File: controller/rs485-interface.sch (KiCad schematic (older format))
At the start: 4 parts

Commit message: Add more stuff to controller, start sourcing parts
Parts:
- gave numbers to parts that had none: 4
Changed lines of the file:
@@
 LIBS:mic-parts
 LIBS:controller-cache
-LIBS:line-interface-cache
 EELAYER 26 0
 EELAYER END
 $Descr A4 11693 8268
 encoding utf-8
-Sheet 4 6
+Sheet 3 10
 Title "Digital soil moisture sensor"
 Date "Tue 17 Feb 2015"
@@
 $EndDescr
 $Comp
-L SP3481EN U?
+L SP3481EN U3
 U 1 1 58C048AA
 P 6000 3600
-F 0 "U?" H 5700 3950 50  0000 L CNN
+F 0 "U3" H 5700 3950 50  0000 L CNN
 F 1 "SN65HVD72" H 6100 3950 50  0000 L CNN
 F 2 "Housings_SOIC:SOIC-8_3.9x4.9mm_Pitch1.27mm" H 6000 3600 50  0001 C CIN
@@
 $EndComp
 $Comp
-L C C?
+L C C20
 U 1 1 58C048AB
 P 4800 2700
-F 0 "C?" H 4850 2800 50  0000 L CNN
+F 0 "C20" H 4850 2800 50  0000 L CNN
 F 1 "1u" H 4850 2600 50  0000 L CNN
 F 2 "Capacitors_SMD:C_0603" H 4838 2550 30  0001 C CNN
@@
 Connection ~ 6000 4150
 $Comp
-L CONN_01X04 J?
+L CONN_01X04 J21
 U 1 1 58C08A57
 P 7400 3600
-F 0 "J?" H 7478 3641 50  0000 L CNN
+F 0 "J21" H 7478 3641 50  0000 L CNN
 F 1 "CONN_01X04" H 7478 3550 50  0000 L CNN
 F 2 "" H -400 250 50  0001 C CNN
@@
 VCC_HIGH
 $Comp
-L Fuse F?
+L Fuse F1
 U 1 1 58C08BC1
 P 7200 3150
-F 0 "F?" H 7260 3196 50  0000 L CNN
+F 0 "F1" H 7260 3196 50  0000 L CNN
 F 1 "Fuse" H 7260 3105 50  0000 L CNN
 F 2 "" V -1620 0   50  0001 C CNN

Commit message: Change gas pedal interface so that it supports going up and down from the middle voltage so that it's compatible with Linde forklift gas mechanism
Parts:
- C20: footprint Capacitors_SMD:C_0603 -> Capacitors_SMD:C_0603_HandSoldering
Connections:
- net VCC renamed +5V
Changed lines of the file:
@@
 F 0 "C20" H 4850 2800 50  0000 L CNN
 F 1 "1u" H 4850 2600 50  0000 L CNN
-F 2 "Capacitors_SMD:C_0603" H 4838 2550 30  0001 C CNN
+F 2 "Capacitors_SMD:C_0603_HandSoldering" H 4838 2550 30  0001 C CNN
 F 3 "" H 4800 2700 60  0000 C CNN
 	1    4800 2700
@@
 ~RE
 Text HLabel 4800 2350 0    60   Input ~ 0
-VCC
++5V
 Wire Wire Line
 	4800 2550 4800 2350

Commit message: More or less final controller board
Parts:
- added C34: 470u, Capacitors_ThroughHole:CP_Radial_D16.0mm_P7.50mm, symbol CP1
- added C35: 1u, Capacitors_SMD:C_0603_HandSoldering, symbol C
- added R57, R58: 1k, Resistors_SMD:R_0603_HandSoldering, symbol R
- added R59: 100k, Resistors_SMD:R_0603_HandSoldering, symbol R
- F1: footprint (none) -> smalsiukas-footpints:Automotive-Fuse-Holder; Distributor (none) -> 1586596; Manufacturer (none) -> ?; PartNo (none) -> ?
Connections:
- net +5V: now also R59.1
- net GND: now also C34.2, C35.2
- net RX: now also R57.1, R57.2
- net TX: now also R58.1, R58.2
- net ~RE: now also R59.2
- net at F1.2, J21.1 (P1): now also C34.1, C35.1
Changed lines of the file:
@@
 LIBS:valves
 LIBS:mic-parts
+LIBS:shield_arduino
 LIBS:controller-cache
 EELAYER 26 0
@@
 RS485B
 Wire Wire Line
-	6000 3200 6000 2550
-Wire Wire Line
-	6000 2550 4800 2550
+	6000 2550 6000 3200
+Wire Wire Line
+	4800 2550 6000 2550
 Wire Wire Line
 	6400 3500 7050 3500
@@
 	5600 3500 5600 3700
 Wire Wire Line
-	5600 3600 5250 3600
+	4450 3600 5600 3600
 Connection ~ 5600 3600
 Text Label 5250 3400 0    60   ~ 0
@@
 Text Label 5250 3600 0    60   ~ 0
 ~RE
-Text HLabel 5250 3400 0    60   Input ~ 0
+Text HLabel 4450 3400 0    60   Input ~ 0
 RX
-Text HLabel 5250 3800 0    60   Input ~ 0
+Text HLabel 4450 3800 0    60   Input ~ 0
 TX
-Text HLabel 5250 3600 0    60   Input ~ 0
+Text HLabel 4450 3600 0    60   Input ~ 0
 ~RE
 Text HLabel 4800 2350 0    60   Input ~ 0
@@
 Wire Wire Line
 	7200 4150 7200 3750
-Text HLabel 7200 2900 2    60   Input ~ 0
+Text HLabel 7200 2100 2    60   Input ~ 0
 VCC_HIGH
+Wire Wire Line
+	7200 2100 7200 2200
+Wire Wire Line
+	7200 2500 7200 3450
 $Comp
 L Fuse F1
-U 1 1 58C08BC1
-P 7200 3150
-F 0 "F1" H 7260 3196 50  0000 L CNN
-F 1 "Fuse" H 7260 3105 50  0000 L CNN
-F 2 "" V -1620 0   50  0001 C CNN
-F 3 "" H -1550 0   50  0001 C CNN
-	1    7200 3150
-	1    0    0    -1
-$EndComp
-Wire Wire Line
-	7200 2900 7200 3000
-Wire Wire Line
-	7200 3300 7200 3450
+U 1 1 58C9F8B4
+P 7200 2350
+F 0 "F1" H 7260 2396 50  0000 L CNN
+F 1 "Fuse" H 7260 2305 50  0000 L CNN
+F 2 "smalsiukas-footpints:Automotive-Fuse-Holder" V 4180 700 50  0001 C CNN
+F 3 "" H 4250 700 50  0001 C CNN
+F 4 "?" H 7200 2350 60  0001 C CNN "PartNo"
+F 5 "?" H 7200 2350 60  0001 C CNN "Manufacturer"
+F 6 "1586596" H 7200 2350 60  0001 C CNN "Distributor"
+	1    7200 2350
+	1    0    0    -1
+$EndComp
+$Comp
+L CP1 C34
+U 1 1 58C9FD4F
+P 6850 3000
+F 0 "C34" H 6965 3046 50  0000 L CNN
+F 1 "470u" H 6965 2955 50  0000 L CNN
+F 2 "Capacitors_ThroughHole:CP_Radial_D16.0mm_P7.50mm" H 1700 1250 50  0001 C CNN
+F 3 "" H 1700 1250 50  0001 C CNN
+F 4 "ECA2AAM471X" H 6850 3000 60  0001 C CNN "PartNo"
+F 5 "PANASONIC" H 6850 3000 60  0001 C CNN "Manufacturer"
+F 6 "8767696" H 6850 3000 60  0001 C CNN "Distributor"
+	1    6850 3000
+	-1   0    0    -1
+$EndComp
+Wire Wire Line
+	6850 2850 7200 2850
+Connection ~ 7200 2850
+Wire Wire Line
+	6850 3150 6850 4150
+Connection ~ 6850 4150
+$Comp
+L GND #PWR09
+U 1 1 58C9FF15
+P 6850 4150
+F 0 "#PWR09" H 6850 3900 50  0001 C CNN
+F 1 "GND" H 6855 3977 50  0000 C CNN
+F 2 "" H 6850 4150 50  0001 C CNN
+F 3 "" H 6850 4150 50  0001 C CNN
+	1    6850 4150
+	1    0    0    -1
+$EndComp
+$Comp
+L C C35
+U 1 1 58CA11C9
+P 7050 3000
+F 0 "C35" H 7100 3100 50  0000 L CNN
+F 1 "1u" H 7100 2900 50  0000 L CNN
+F 2 "Capacitors_SMD:C_0603_HandSoldering" H 7088 2850 30  0001 C CNN
+F 3 "" H 7050 3000 60  0000 C CNN
+	1    7050 3000
+	1    0    0    -1
+$EndComp
+Wire Wire Line
+	7050 3150 6850 3150
+Connection ~ 7050 2850
+$Comp
+L R R59
+U 1 1 58CB3B0F
+P 5450 2950
+F 0 "R59" H 5519 2996 50  0000 L CNN
+F 1 "100k" H 5519 2905 50  0000 L CNN
+F 2 "Resistors_SMD:R_0603_HandSoldering" V 1830 450 50  0001 C CNN
+F 3 "" H 1900 450 50  0001 C CNN
+	1    5450 2950
+	-1   0    0    -1
+$EndComp
+Wire Wire Line
+	5450 2800 5450 2550
+Connection ~ 5450 2550
+Wire Wire Line
+	5450 3100 5450 3600
+Connection ~ 5450 3600
+$Comp
+L R R58
+U 1 1 58CB3BD1
+P 5100 3800
+F 0 "R58" V 5215 3800 50  0000 C CNN
+F 1 "1k" V 5306 3800 50  0000 C CNN
+F 2 "Resistors_SMD:R_0603_HandSoldering" V 1480 1300 50  0001 C CNN
+F 3 "" H 1550 1300 50  0001 C CNN
+	1    5100 3800
+	0    1    1    0
+$EndComp
+$Comp
+L R R57
+U 1 1 58CB3CD2
+P 5100 3400
+F 0 "R57" V 4893 3400 50  0000 C CNN
+F 1 "1k" V 4984 3400 50  0000 C CNN
+F 2 "Resistors_SMD:R_0603_HandSoldering" V 1480 900 50  0001 C CNN
+F 3 "" H 1550 900 50  0001 C CNN
+	1    5100 3400
+	0    -1   1    0
+$EndComp
+Wire Wire Line
+	4950 3400 4450 3400
+Wire Wire Line
+	4950 3800 4450 3800
 $EndSCHEMATC

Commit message: Finish the routing, add some significant fixes: *correct to-252 pin numbering * longer pads for relays * fix footprint of the optocouplers
Also finish the routing
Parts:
- J21: footprint (none) -> Connectors_JST:JST_EH_B04B-EH-A_04x2.50mm_Straight; Distributor (none) -> 1830714, 1830708, 1863249; Manufacturer (none) -> ?; PartNo (none) -> ?
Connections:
- net RX: no longer R57.2, U3.1 (RO)
- net TX: no longer R58.1, U3.4 (DI)
- new net: R57.2, U3.1 (RO)
- new net: R58.1, U3.4 (DI)
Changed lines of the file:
@@
 	4450 3600 5600 3600
 Connection ~ 5600 3600
-Text Label 5250 3400 0    60   ~ 0
-RX
-Text Label 5250 3800 0    60   ~ 0
-TX
-Text Label 5250 3600 0    60   ~ 0
-~RE
 Text HLabel 4450 3400 0    60   Input ~ 0
 RX
@@
 F 0 "J21" H 7478 3641 50  0000 L CNN
 F 1 "CONN_01X04" H 7478 3550 50  0000 L CNN
-F 2 "" H -400 250 50  0001 C CNN
+F 2 "Connectors_JST:JST_EH_B04B-EH-A_04x2.50mm_Straight" H -400 250 50  0001 C CNN
 F 3 "" H -400 250 50  0001 C CNN
+F 4 "?" H 7400 3600 60  0001 C CNN "PartNo"
+F 5 "?" H 7400 3600 60  0001 C CNN "Manufacturer"
+F 6 "1830714, 1830708, 1863249" H 7400 3600 60  0001 C CNN "Distributor"
 	1    7400 3600
 	1    0    0    -1

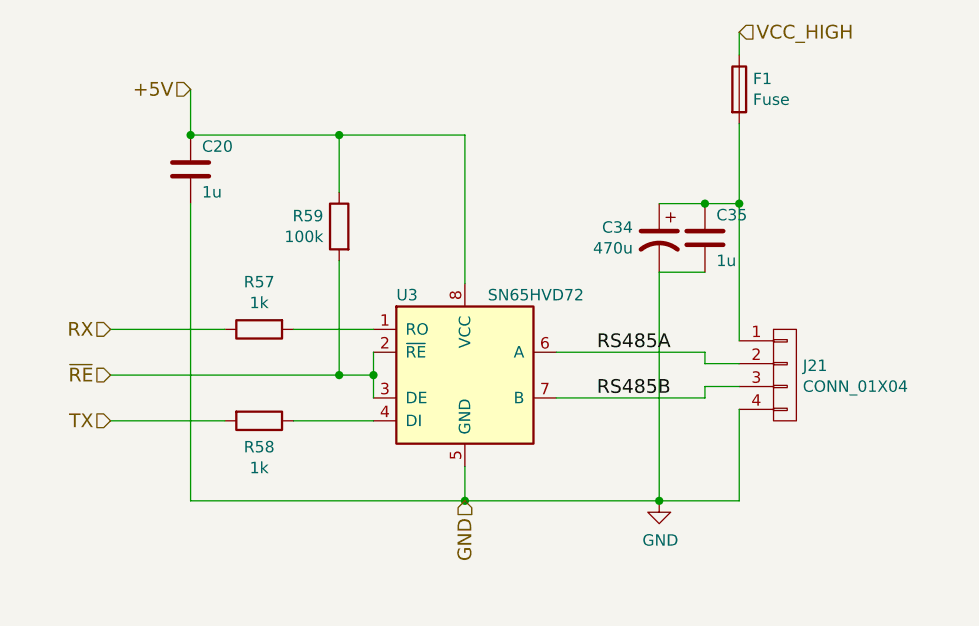
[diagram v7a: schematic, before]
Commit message: add comments with fixes I had to make
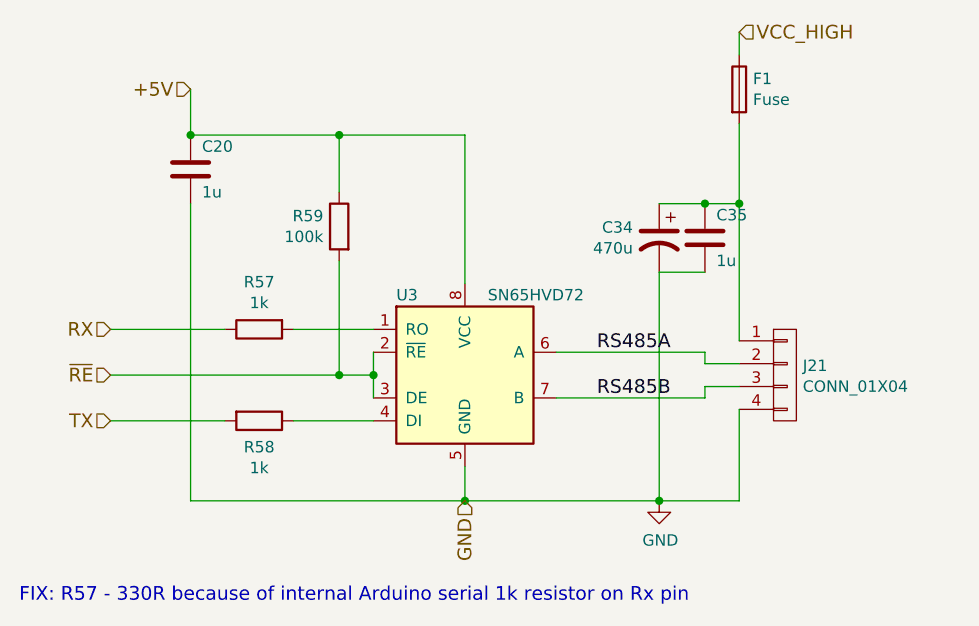
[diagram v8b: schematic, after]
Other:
- note added: "FIX: R57 - 330R because of internal Arduino serial 1k resistor on Rx pin"
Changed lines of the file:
@@
 Wire Wire Line
 	4950 3800 4450 3800
+Text Notes 4050 4600 0    60   ~ 0
+FIX: R57 - 330R because of internal Arduino serial 1k resistor on Rx pin
 $EndSCHEMATC
